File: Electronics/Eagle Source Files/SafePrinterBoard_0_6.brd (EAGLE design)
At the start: 68.6 x 53.3 mm, 31 parts, among them U1 ARDUINOR3-BPLACE

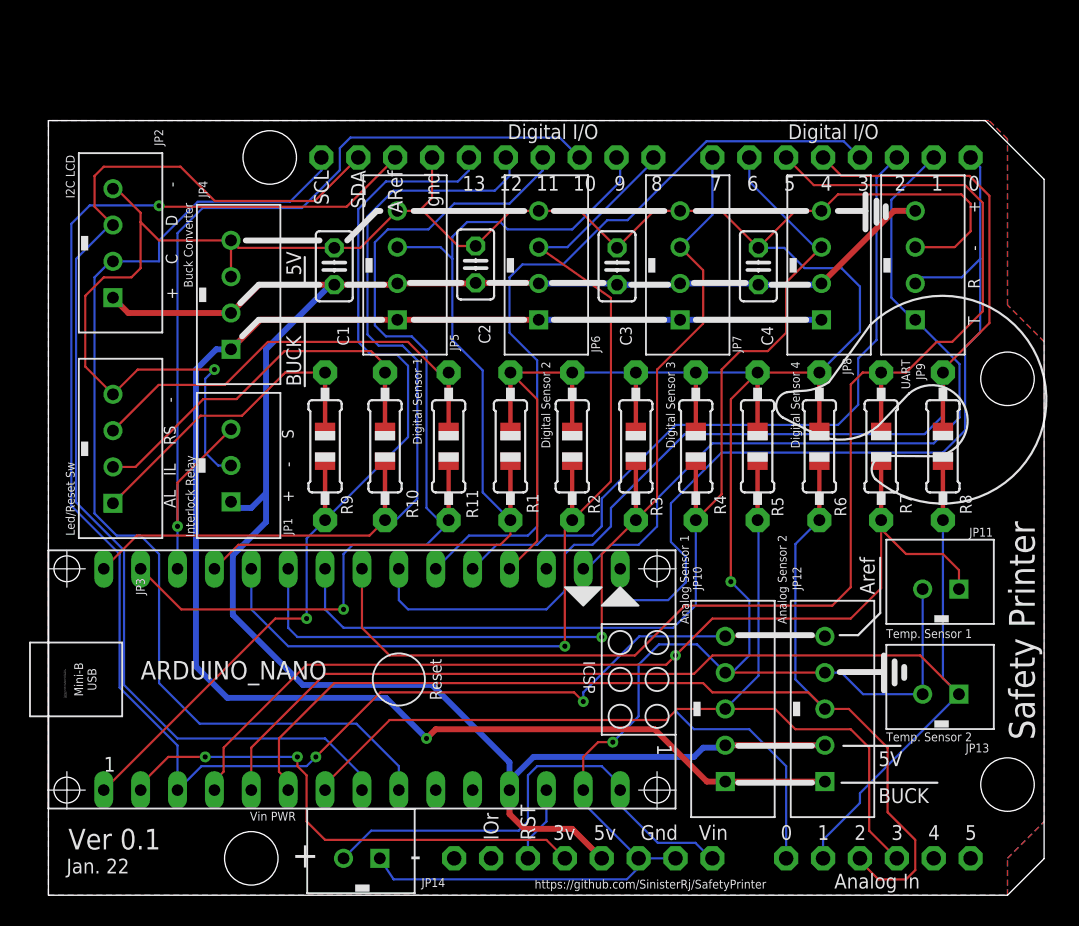
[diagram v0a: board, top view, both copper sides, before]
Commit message: Board Ver 0.6
1) Adds capacitor to avoid autoreset upon serial connection;
2) Removes UART connector;
3) Adds neopixel support for alarm and trip LEDs;
4) Removes some unused holes;
5) Rearranges some connectors to avoid Arduino UNO USB connector short circuit.
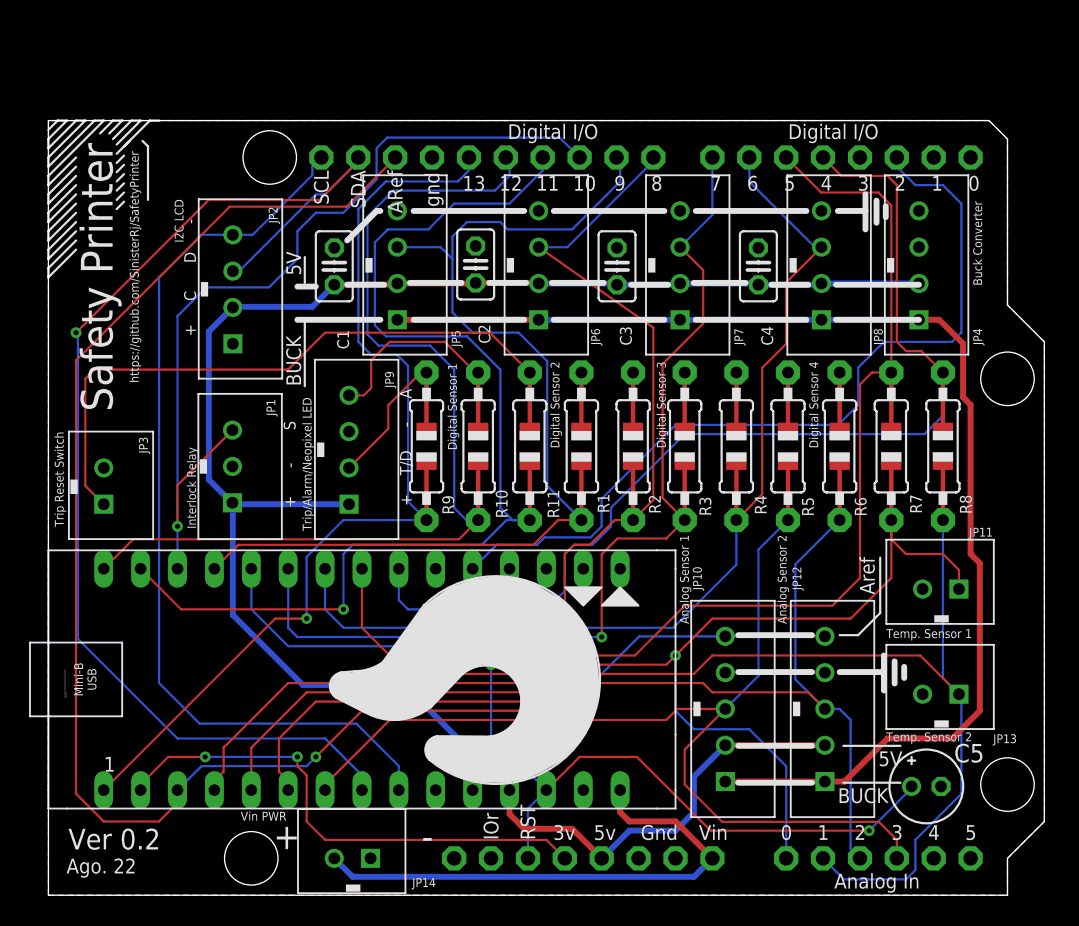
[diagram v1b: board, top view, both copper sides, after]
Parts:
- added C5: 10uF, rcl:E2-5
- JP3: value Led/Reset Sw -> Trip Reset Switch; device RodrigoCesar:B4B-PH-K-S -> RodrigoCesar:B2B-PH-K-S
- JP9: value UART -> Trip/Alarm/Neopixel LED
- R9: value 470 -> 330 or 470
- moved JP4 47.4 mm to (81.5, 48.5)
- moved JP9 41.0 mm to (42.3, 35.8)
- moved JP2 8.84 mm to (34.3, 46.9)
- moved R9 6.98 mm to (47.6, 39.8)
- moved R10 6.41 mm to (51.2, 39.8)
- moved R11 5.59 mm to (54.7, 39.8)
- moved R1 4.89 mm to (58.3, 39.8)
- moved R2 4.19 mm to (61.8, 39.8)
- moved R3 3.37 mm to (65.4, 39.8)
- moved R4 2.79 mm to (69.0, 39.8)
- moved JP3 2.51 mm to (25.4, 38.3)
- moved R5 2.10 mm to (72.5, 39.8)
- moved R6 1.40 mm to (76.1, 39.8)
- moved R7 0.70 mm to (79.6, 39.8)
- moved JP14 0.63 mm to (41.3, 11.4)
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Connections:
- removed net N$17: ARDUINO_NANO.17, JP9.1, U1.D1
- removed net N$18: ARDUINO_NANO.16, JP9.2, U1.D0
- removed net N$25: ARDUINO_NANO.21, U1.D3
- removed net N$26: ARDUINO_NANO.20, U1.D2
- net +5V: now also JP2.2, JP9.1; no longer JP2.1, JP9.4
- net GND4: now also C5.-, JP2.1, JP3.2; no longer JP2.4, JP3.4
- net N$10: now also JP2.4; no longer JP2.2
- net N$13: now also JP9.4, R10.2; no longer JP3.1, R9.2
- net N$19: now also ARDUINO_NANO.20, C5.+, U1.D2
- net N$27: now also JP3.1; no longer JP3.3
- net N$3: now also JP9.2, R9.2; no longer JP3.2, R10.2
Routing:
- net GND4: track 255.4 -> 0.00 mm, vias 3 -> 0
- net N$19: track 5.23 -> 110.1 mm, vias 0 -> 2
- net N$18: track 59.7 -> 0.00 mm
- net N$25: track 54.6 -> 0.00 mm
- net N$17: track 52.5 -> 0.00 mm
- net N$26: track 50.5 -> 0.00 mm
- net +12V: track 112.1 -> 84.9 mm, vias 1 -> 0
- net N$27: track 26.5 -> 42.2 mm
- net N$3: track 23.0 -> 9.00 mm
- net +5V: track 144.7 -> 131.9 mm
- net N$9: track 64.4 -> 74.7 mm
- net N$12: track 87.9 -> 78.3 mm
- net N$8: track 57.7 -> 66.1 mm
- net N$10: track 71.7 -> 63.4 mm
- net N$6: track 63.0 -> 71.1 mm
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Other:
- outline, holes or cut-outs redrawn
- board text added: "+ T/D - A"
- board text added: "Ago. 22"
- board text added: "Ver 0.2"
- board text added: "afetypri"
- board text added: "afetyprintersafetyprintersafetyprintersafe"
- board text added: "ersafetyprintersafetyprintersafetyprintersaf"
- board text added: "etyprintersafetyp"
- board text added: "etyprintersafetyprintersafetyprin"
- board text added: "fetyprinters"
- board text added: "fetyprintersafetyprintersafetyprinter"
- board text added: "intersafe"
- board text added: "intersafetyprintersafetyprintersafetypri"
- board text added: "nters"
- board text added: "ntersafetyprintersafetyprintersafetyprinters"
- board text added: "printersafetyprinte"
- board text added: "printersafetyprintersafetyprint"
- board text added: "rintersafetypr"
- board text added: "rintersafetyprintersafetyprintersaf"
- board text added: "rsafetyprintersafetyprintersafetyprintersafet"
- board text added: "saf"
- board text added: "safetyprintersafetyprintersafetyprintersafet"
- board text added: "t"
- board text added: "tersafetyprintersafetyprintersafetyprintersa"
- board text added: "typrintersafetyprinte"
- board text added: "typrintersafetyprintersafety"
- board text added: "yprintersafetyprintersa"
- board text added: "yprintersafetyprintersafet"
- board text removed: "AL IL RS -"
- board text removed: "Jan. 22"
- board text removed: "T R - +"
- board text removed: "Ver 0.1"
